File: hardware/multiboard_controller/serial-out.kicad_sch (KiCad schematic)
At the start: 1 part, among them J10 DE9_Plug_MountingHoles

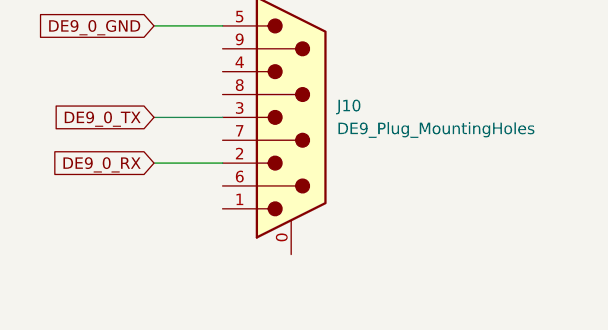
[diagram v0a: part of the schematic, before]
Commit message: Choose switches for UART muxing. USB-to-UART schematic WIP.
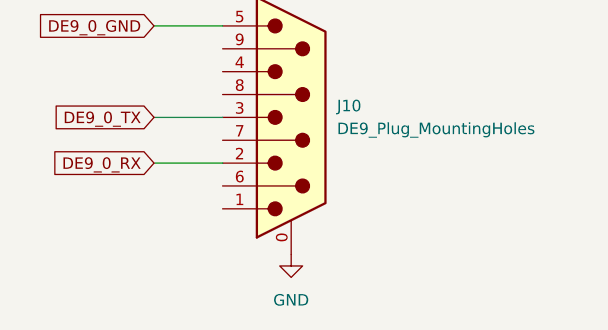
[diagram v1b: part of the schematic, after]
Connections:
- net GND: now reaches J10.0 (PAD)
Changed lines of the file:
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@@
+	)
+	(symbol
+		(lib_id "power:GND")
+		(at 66.04 62.23 0)
+		(unit 1)
+		(exclude_from_sim no)
+		(in_bom yes)
+		(on_board yes)
+		(dnp no)
+		(fields_autoplaced yes)
+		(property "Reference" "#PWR032"
+			(at 66.04 68.58 0)
+			(effects
+				(font
+					(size 1.27 1.27)
+				)
+				(hide yes)
+			)
+		)
+		(property "Value" "GND"
+			(at 66.04 67.31 0)
+			(effects
+				(font
+					(size 1.27 1.27)
+				)
+			)
+		)
+		(property "Footprint" ""
+			(at 66.04 62.23 0)
+			(effects
+				(font
+					(size 1.27 1.27)
+				)
+				(hide yes)
+			)
+		)
+		(property "Datasheet" ""
+			(at 66.04 62.23 0)
+			(effects
+				(font
+					(size 1.27 1.27)
+				)
+				(hide yes)
+			)
+		)
+		(property "Description" "Power symbol creates a global label with name \"GND\" , ground"
+			(at 66.04 62.23 0)
+			(effects
+				(font
+					(size 1.27 1.27)
+				)
+				(hide yes)
+			)
+		)
+		(pin "1"
+		)
+		(instances
+			(project ""
+				(path "/0fe19ce7-810a-40c6-903d-4212edc122f9/e8db22f7-77fb-46ba-a7ea-4554afbfcc59"
+					(reference "#PWR032")
+					(unit 1)
+				)
+			)
+		)
 	)
 	(symbol

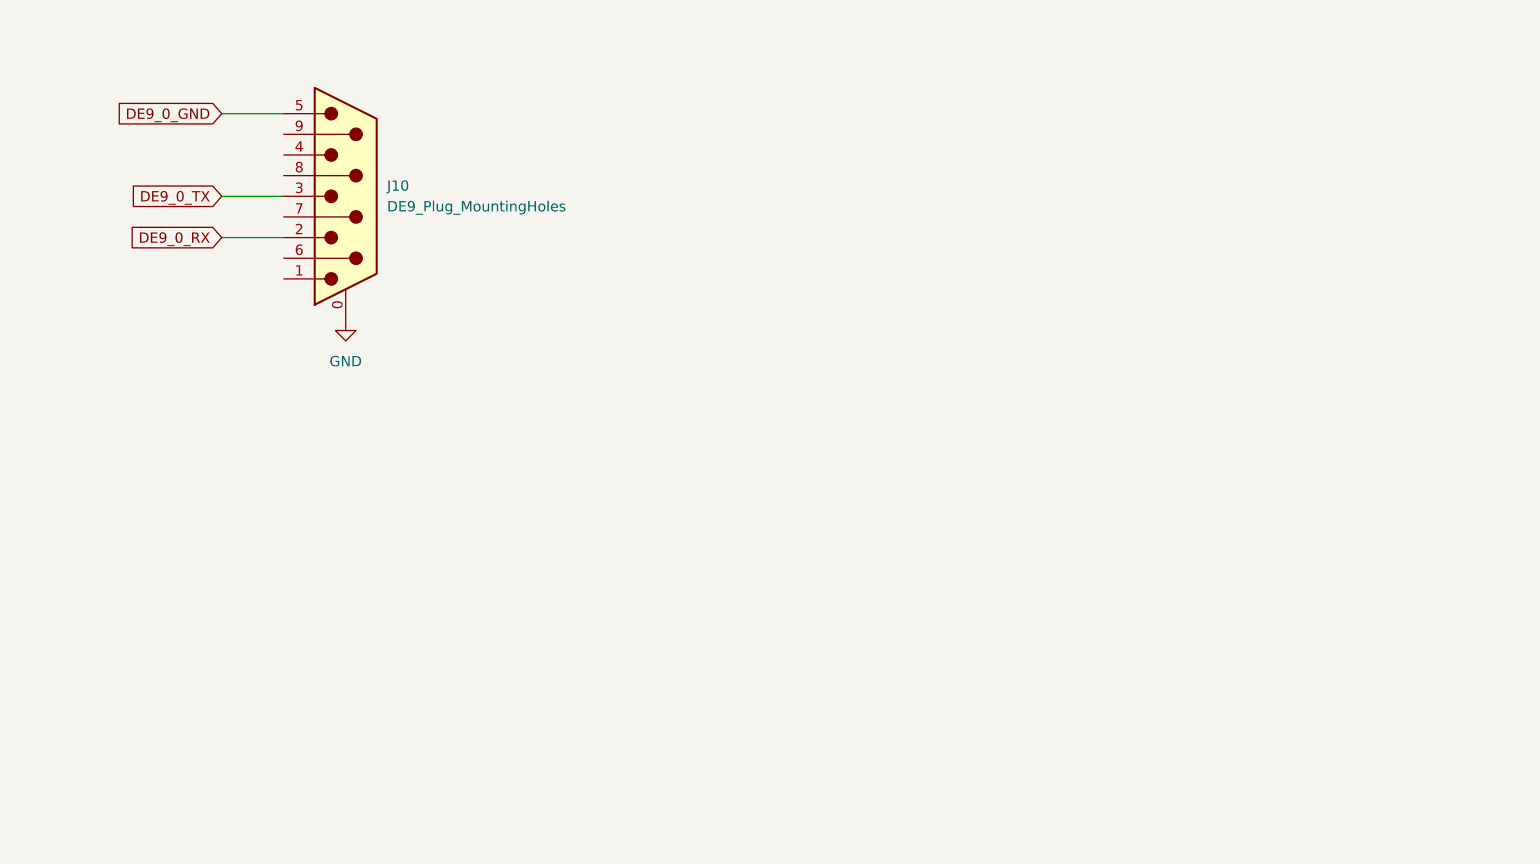
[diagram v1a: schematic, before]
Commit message: Adding final connectors and general cleanup.
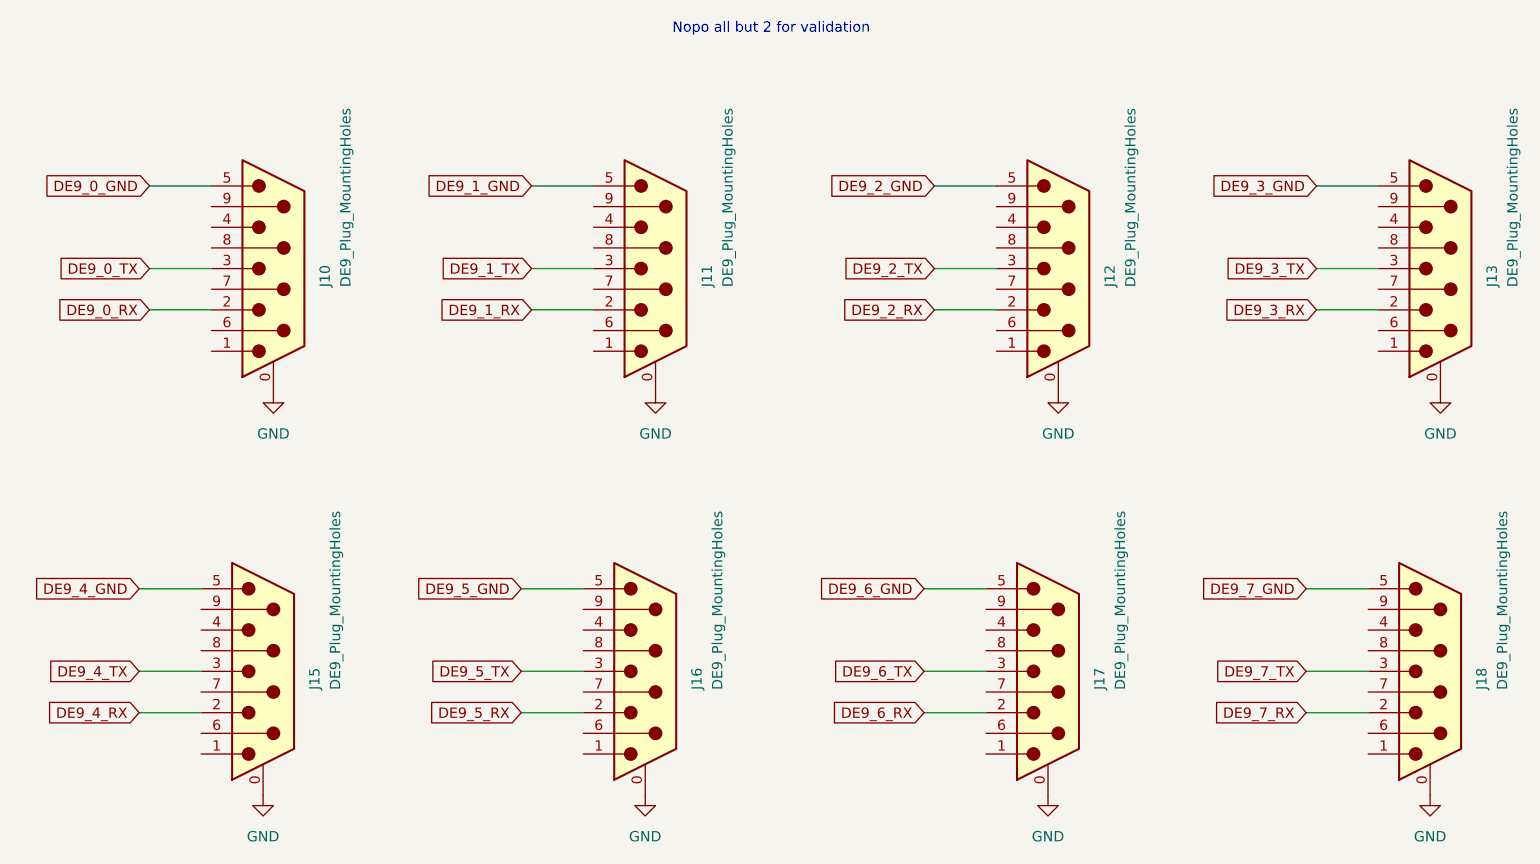
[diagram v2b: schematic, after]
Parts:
- added J11, J12, J13, J15, J16, J17, J18: DE9_Plug_MountingHoles, symbol Connector:DE9_Plug_MountingHoles
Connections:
- net GND: now also J11.0 (PAD), J12.0 (PAD), J13.0 (PAD), J15.0 (PAD), J16.0 (PAD), J17.0 (PAD), J18.0 (PAD)
- new net DE9_1_GND: J11.5
- new net DE9_1_RX: J11.2
- new net DE9_1_TX: J11.3
- new net DE9_2_GND: J12.5
- new net DE9_2_RX: J12.2
- new net DE9_2_TX: J12.3
- new net DE9_3_GND: J13.5
- new net DE9_3_RX: J13.2
- new net DE9_3_TX: J13.3
- new net DE9_4_GND: J15.5
- new net DE9_4_RX: J15.2
- new net DE9_4_TX: J15.3
- new net DE9_5_GND: J16.5
- new net DE9_5_RX: J16.2
- new net DE9_5_TX: J16.3
- new net DE9_6_GND: J17.5
- new net DE9_6_RX: J17.2
- new net DE9_6_TX: J17.3
- new net DE9_7_GND: J18.5
- new net DE9_7_RX: J18.2
- new net DE9_7_TX: J18.3
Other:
- note added: "Nopo all but 2 for validation"
- moved on the sheet: J10

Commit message: Starting layout
Add serial ground connections, add footprint libraries, start layout.
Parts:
- J10: footprint (none) -> all-footprints:ASSMANN_A-DS_09_A_KG-T2S
- J11, J12, J13, J15, J16, J17, J18: footprint (none) -> all-footprints:ASSMANN_A-DS_09_A_KG-T2S; now not fitted
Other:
- note added: "Nop all but 2 for validation"
- note removed: "Nopo all but 2 for validation"
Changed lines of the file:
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@@
 		)
 	)
-	(text "Nopo all but 2 for validation\n"
+	(text "Nop all but 2 for validation\n"
 		(exclude_from_sim no)
 		(at 118.364 26.416 0)
@@
 		(in_bom yes)
 		(on_board yes)
-		(dnp no)
+		(dnp yes)
 		(property "Reference" "J12"
 			(at 160.02 58.166 90)
@@
 			)
 		)
-		(property "Footprint" ""
+		(property "Footprint" "all-footprints:ASSMANN_A-DS_09_A_KG-T2S"
 			(at 153.67 55.88 0)
 			(effects
@@
 		(in_bom yes)
 		(on_board yes)
-		(dnp no)
+		(dnp yes)
 		(property "Reference" "J18"
 			(at 205.74 107.696 90)
@@
 			)
 		)
-		(property "Footprint" ""
+		(property "Footprint" "all-footprints:ASSMANN_A-DS_09_A_KG-T2S"
 			(at 199.39 105.41 0)
 			(effects
@@
 		(in_bom yes)
 		(on_board yes)
-		(dnp no)
+		(dnp yes)
 		(property "Reference" "J16"
 			(at 109.22 107.696 90)
@@
 			)
 		)
-		(property "Footprint" ""
+		(property "Footprint" "all-footprints:ASSMANN_A-DS_09_A_KG-T2S"
 			(at 102.87 105.41 0)
 			(effects
@@
 		(in_bom yes)
 		(on_board yes)
-		(dnp no)
+		(dnp yes)
 		(property "Reference" "J15"
 			(at 62.23 107.696 90)
@@
 			)
 		)
-		(property "Footprint" ""
+		(property "Footprint" "all-footprints:ASSMANN_A-DS_09_A_KG-T2S"
 			(at 55.88 105.41 0)
 			(effects
@@
 		(in_bom yes)
 		(on_board yes)
-		(dnp no)
+		(dnp yes)
 		(fields_autoplaced yes)
 		(property "Reference" "#PWR044"
@@
 		(in_bom yes)
 		(on_board yes)
-		(dnp no)
+		(dnp yes)
 		(property "Reference" "J11"
 			(at 110.49 58.166 90)
@@
 			)
 		)
-		(property "Footprint" ""
+		(property "Footprint" "all-footprints:ASSMANN_A-DS_09_A_KG-T2S"
 			(at 104.14 55.88 0)
 			(effects
@@
 		(in_bom yes)
 		(on_board yes)
-		(dnp no)
+		(dnp yes)
 		(fields_autoplaced yes)
 		(property "Reference" "#PWR049"
@@
 		(in_bom yes)
 		(on_board yes)
-		(dnp no)
+		(dnp yes)
 		(fields_autoplaced yes)
 		(property "Reference" "#PWR042"
@@
 		(in_bom yes)
 		(on_board yes)
-		(dnp no)
+		(dnp yes)
 		(property "Reference" "J13"
 			(at 207.01 58.166 90)
@@
 			)
 		)
-		(property "Footprint" ""
+		(property "Footprint" "all-footprints:ASSMANN_A-DS_09_A_KG-T2S"
 			(at 200.66 55.88 0)
 			(effects
@@
 		(in_bom yes)
 		(on_board yes)
-		(dnp no)
+		(dnp yes)
 		(fields_autoplaced yes)
 		(property "Reference" "#PWR046"
@@
 		(in_bom yes)
 		(on_board yes)
-		(dnp no)
+		(dnp yes)
 		(fields_autoplaced yes)
 		(property "Reference" "#PWR048"
@@
 		(in_bom yes)
 		(on_board yes)
-		(dnp no)
+		(dnp yes)
 		(property "Reference" "J17"
 			(at 158.75 107.696 90)
@@
 			)
 		)
-		(property "Footprint" ""
+		(property "Footprint" "all-footprints:ASSMANN_A-DS_09_A_KG-T2S"
 			(at 152.4 105.41 0)
 			(effects
@@
 			)
 		)
-		(property "Footprint" ""
+		(property "Footprint" "all-footprints:ASSMANN_A-DS_09_A_KG-T2S"
 			(at 57.15 55.88 0)
 			(effects
@@
 		(in_bom yes)
 		(on_board yes)
-		(dnp no)
+		(dnp yes)
 		(fields_autoplaced yes)
 		(property "Reference" "#PWR047"
@@
 		(in_bom yes)
 		(on_board yes)
-		(dnp no)
+		(dnp yes)
 		(fields_autoplaced yes)
 		(property "Reference" "#PWR043"
